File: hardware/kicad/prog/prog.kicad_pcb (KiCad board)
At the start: 4 copper layers, 174 x 134 mm, 124 parts, among them J1 AES_PROG, J2 Câble PROG-CHA, J3 PROG P, J4 PROG V, U1 AMS1117-3.3, U10 iCE40HX4K-TQ144, U11 W25Q32JVSS, U12 W9825G6KH-6, U13 iCE40HX4K-TQ144, U14 W25Q32JVSS, U15 W9825G6KH-6, U2 AP2112K-1.2, U3 74LVC16244A, U4 74LVC16244A, U5 74LVC16244A, U6 74LVC16245A, U7 74LVC16245A, U8 74AHCT125, U9 74LVC1G07, X1 25 MHz 3,3 V, X2 25 MHz 3,3 V

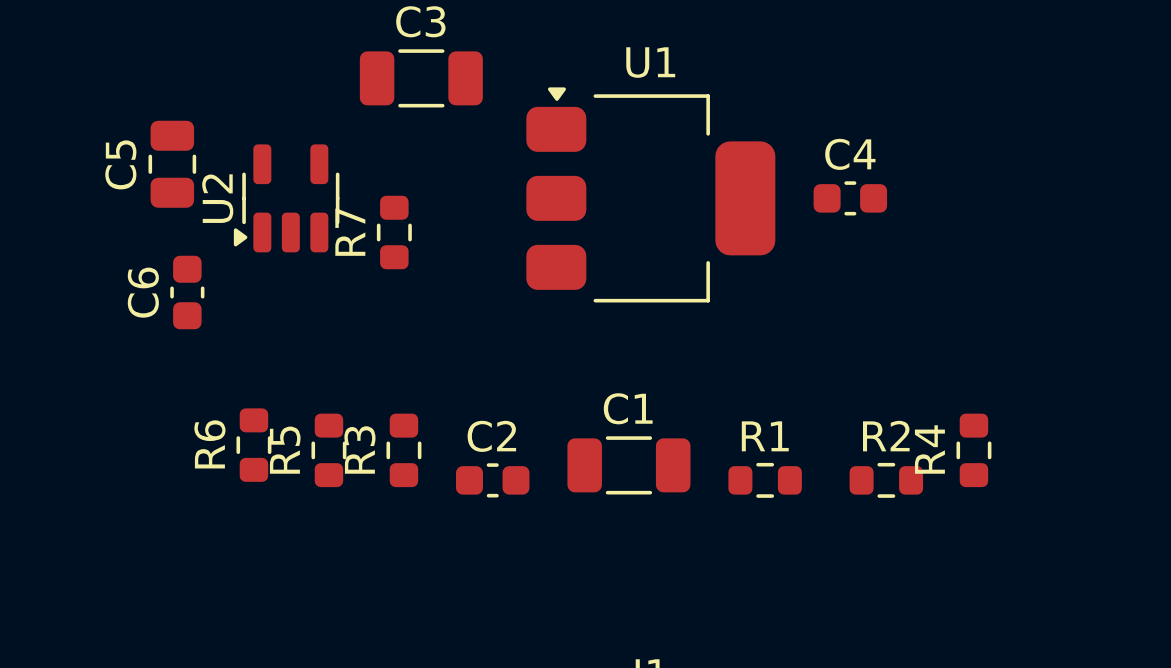
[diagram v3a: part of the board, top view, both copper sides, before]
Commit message: PCB : pistes et isolements de 0,127 mm
Premier routage 4 couches bloqué à 76 liaisons sur la carte PROG avec
0,15 mm ; 0,127 mm (5 mil) reste dans les capacités courantes des
fabricants en 4 couches.

Co-Authored-By: Claude Opus 5.5 <noreply@anthropic.com>
Claude-Session: https://claude.ai/code/session_01WKfXP1YJ8otGxZ5dsY6Agh
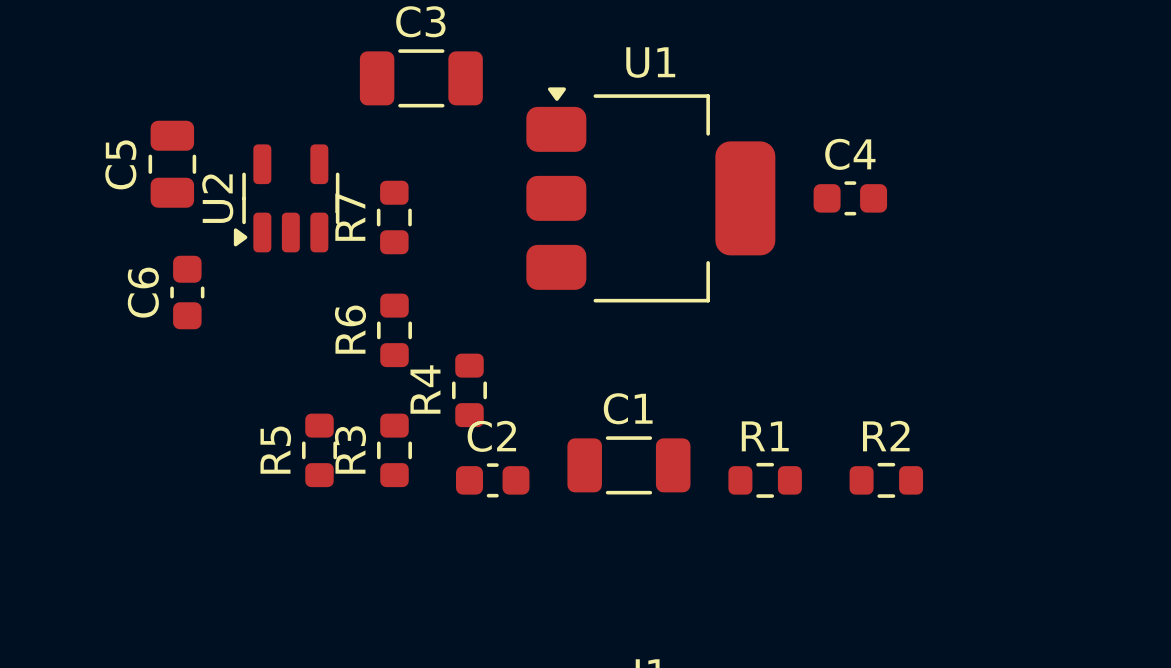
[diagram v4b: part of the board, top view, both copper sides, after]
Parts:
- moved R4 16.9 mm to (144.0, 156.4)
- moved R6 6.05 mm to (141.5, 154.4)
- moved R7 0.50 mm to (141.4, 150.6)
- moved R3 0.31 mm to (141.5, 158.4)
- moved R5 0.31 mm to (139.0, 158.4)

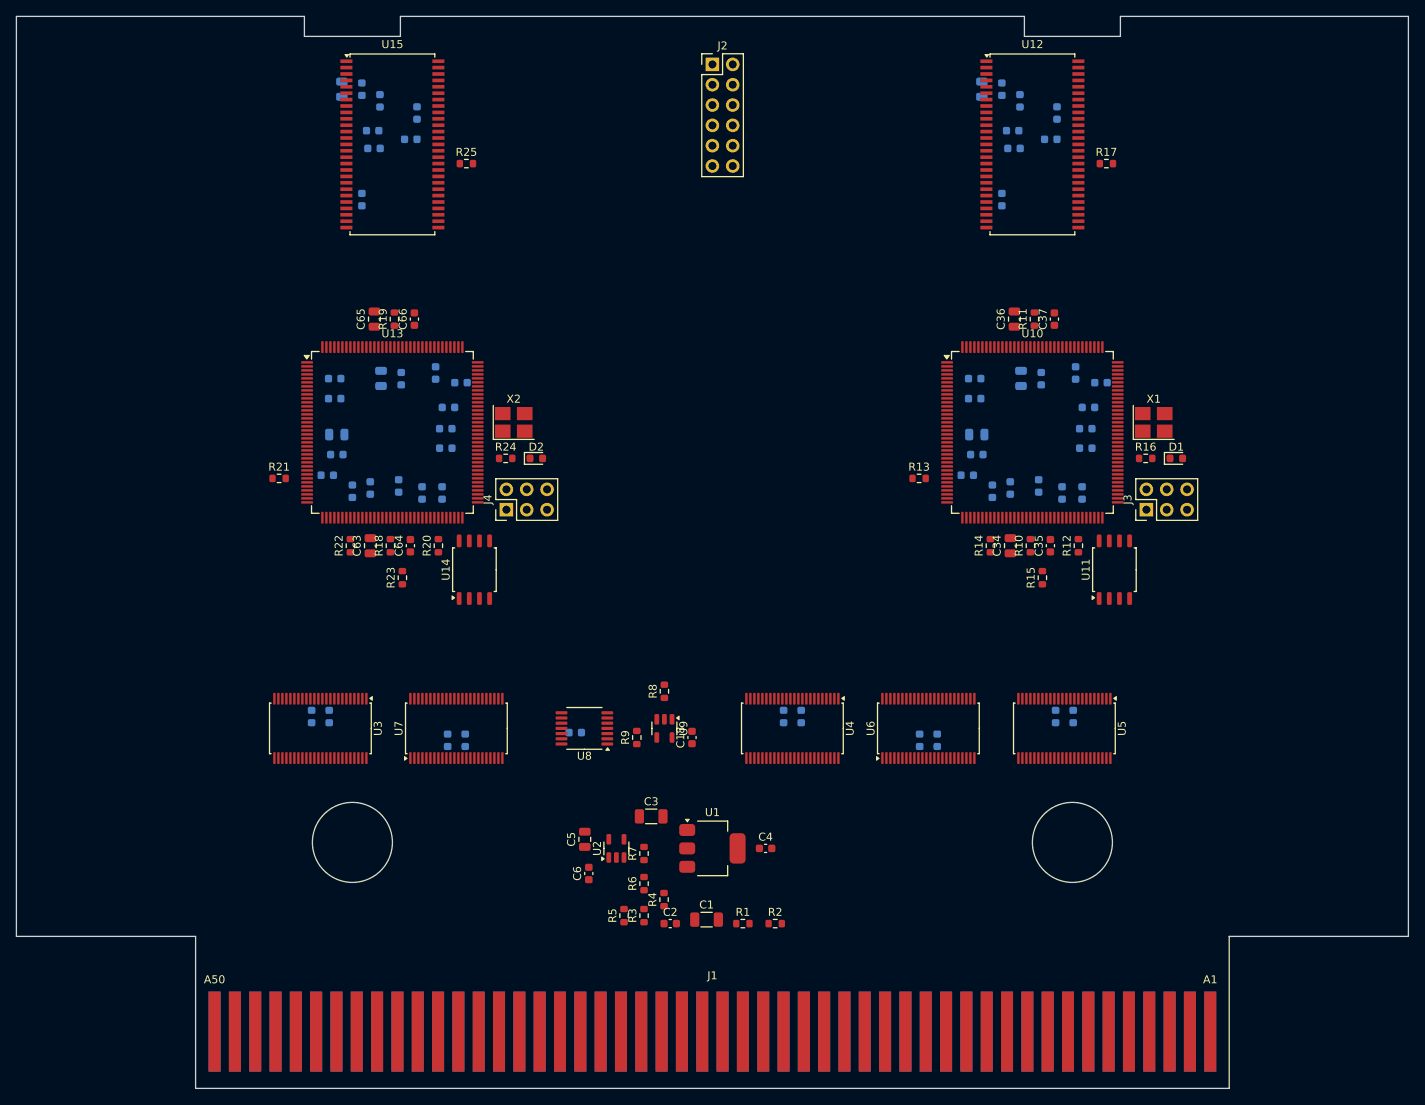
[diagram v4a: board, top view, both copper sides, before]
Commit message: PCB : 9 trous d'entretoise, vias vers les plans, zones interdites
- 9 trous M3 aux mêmes coordonnées sur PROG et CHA (H1-H9) pour relier
  les deux cartes par des entretoises ; 3,5 mm sans composant ni cuivre
  autour.
- Vias de raccordement aux plans (masse, +3V3) posés avant le routage
  pour chaque pastille CMS : au premier routage complet de la carte
  PROG, tous les signaux étaient routés et les 85 liaisons manquantes
  étaient toutes des raccordements aux plans.
- Zones interdites aux pistes autour des trous de la coque et des
  entretoises ; rétrécissement à 0,09 mm admis à l'entrée des broches.
- route.py : DRC par le module pcbnew (kicad-cli 7 n'en a pas), lecture
  de session corrigée.
- Pico descendu de 3 mm (chevauchait le lecteur microSD).

Co-Authored-By: Claude Opus 5.5 <noreply@anthropic.com>
Claude-Session: https://claude.ai/code/session_01WKfXP1YJ8otGxZ5dsY6Agh
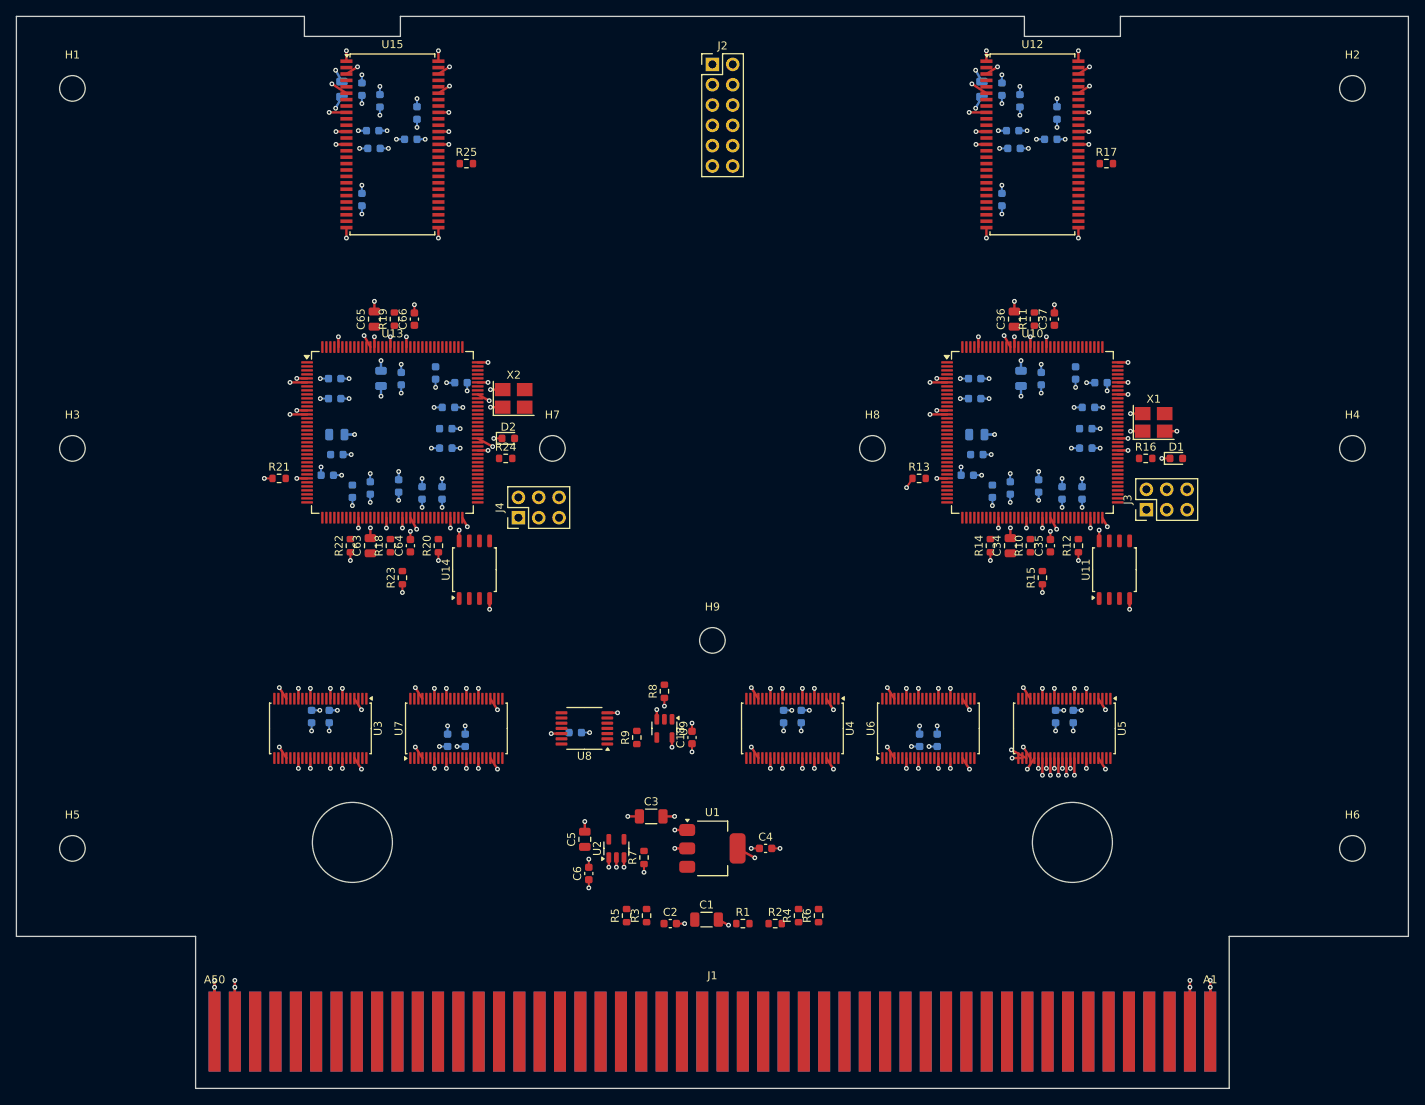
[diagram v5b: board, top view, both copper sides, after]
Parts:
- added H1: Entretoise M3, MountingHole:MountingHole_3.2mm_M3, F.Cu at (70.0, 55.0)
- added H2: Entretoise M3, MountingHole:MountingHole_3.2mm_M3, F.Cu at (230.0, 55.0)
- added H3: Entretoise M3, MountingHole:MountingHole_3.2mm_M3, F.Cu at (70.0, 100.0)
- added H4: Entretoise M3, MountingHole:MountingHole_3.2mm_M3, F.Cu at (230.0, 100.0)
- added H5: Entretoise M3, MountingHole:MountingHole_3.2mm_M3, F.Cu at (70.0, 150.0)
- added H6: Entretoise M3, MountingHole:MountingHole_3.2mm_M3, F.Cu at (230.0, 150.0)
- added H7: Entretoise M3, MountingHole:MountingHole_3.2mm_M3, F.Cu at (130.0, 100.0)
- added H8: Entretoise M3, MountingHole:MountingHole_3.2mm_M3, F.Cu at (170.0, 100.0)
- added H9: Entretoise M3, MountingHole:MountingHole_3.2mm_M3, F.Cu at (150.0, 124.0)
- moved R6 22.2 mm to (163.3, 158.4)
- moved R4 16.9 mm to (160.8, 158.4)
- moved D2 4.30 mm to (124.5, 98.8)
- moved X2 3.00 mm to (125.2, 93.8)
- moved J4 1.80 mm to (125.8, 108.7)
- moved R7 0.50 mm to (141.4, 151.1)
- moved R3 0.31 mm to (141.8, 158.4)
- moved R5 0.31 mm to (139.3, 158.4)
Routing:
- net GND: track 0.00 -> 270.9 mm, vias 0 -> 180
- net +3V3: track 0.00 -> 161.1 mm, vias 0 -> 129

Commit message: Routage : vias vers les plans verrouillés, Freerouting sans sortie des broches ni optimisation
L'import de la session effaçait aussi les vias vers les plans posés par
pcb.py (82 des 85 liaisons manquantes de la carte PROG) : ils sont
désormais verrouillés et conservés. Freerouting ne refait plus la
sortie des broches (près d'une heure perdue sur la carte CHA) ni
l'optimisation finale. Zones interdites limitées aux 4 couches
utilisées ; remplissage et DRC dans un processus à part (second
LoadBoard inutilisable dans le même processus).

Co-Authored-By: Claude Opus 5.5 <noreply@anthropic.com>
Claude-Session: https://claude.ai/code/session_01WKfXP1YJ8otGxZ5dsY6Agh
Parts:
- moved R4 18.0 mm to (143.0, 155.3), turned to 0 degrees
- moved R6 13.1 mm to (150.5, 155.3), turned to 0 degrees
- moved R5 6.74 mm to (143.0, 152.8), turned to 0 degrees
- moved R3 5.95 mm to (146.8, 155.3), turned to 0 degrees
- moved R7 1.50 mm to (141.4, 149.6)

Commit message: FPGA configurés par le RP2350 depuis la carte SD (plus de flash)
- Matériel : flash SPI retirées (4 W25Q32, 12 résistances, 4
  condensateurs). Le bus de liaison arrive sur les broches de
  configuration des iCE40 (LK_SCK -> 70 SCK, LK_IO[0] -> 68 SDI,
  LK_CS_N -> 71 SS), qui redeviennent ces entrées après le démarrage.
  CRESET_N commun aux 4 FPGA, tiré à la masse, piloté par le RP2350
  (GP28) ; câble PROG-CHA en 2 x 7 (CRESET_N + masse). Connecteur 2 x 3
  de secours par FPGA (iceprog -S).
- Firmware : fpga_boot.c (reset commun en mode SPI esclave, envoi des
  SDAES/fpga_*.bin l'un après l'autre, contrôle de CDONE) ; testé sur
  PC (bitstreams reçus à l'identique, FPGA laissés en reset si un
  fichier manque).
- make -C hdl sd : fichiers à copier sur la carte SD.
- PCB : table de placement et références des FPGA mises à jour,
  broches réoptimisées.
Placement-routage des FPGA avec les nouvelles broches : en cours.

Co-Authored-By: Claude Opus 5.5 <noreply@anthropic.com>
Claude-Session: https://claude.ai/code/session_01WKfXP1YJ8otGxZ5dsY6Agh
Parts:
- removed C75: 100n, Capacitor_SMD:C_0603_1608Metric
- removed C76: 10u, Capacitor_SMD:C_0805_2012Metric
- removed R20, R21, R22, R23: 10k, Resistor_SMD:R_0603_1608Metric
- removed R24: 470, Resistor_SMD:R_0603_1608Metric
- removed R25: 33, Resistor_SMD:R_0603_1608Metric
- removed U14: W25Q32JVSS, Package_SO:SOIC-8_5.23x5.23mm_P1.27mm
- removed U15: W9825G6KH-6, Package_SO:TSOP-II-54_22.2x10.16mm_P0.8mm
- C46, C51, C61, C64, C74: value 100n -> 10u; footprint Capacitor_SMD:C_0603_1608Metric -> Capacitor_SMD:C_0805_2012Metric
- C47, C52, C63, C65: value 10u -> 100n; footprint Capacitor_SMD:C_0805_2012Metric -> Capacitor_SMD:C_0603_1608Metric
- C62: moved to F.Cu
- C66: moved to B.Cu
- J2: footprint Connector_PinHeader_2.54mm:PinHeader_2x06_P2.54mm_Vertical -> Connector_PinHeader_2.54mm:PinHeader_2x07_P2.54mm_Vertical
- J3: value PROG P -> CONF P
- J4: value PROG V -> CONF V
- R13: value 10k -> 470
- R14: value 10k -> 33
- R15: value 10k -> 100
- R16: value 470 -> 100
- R17: value 33 -> 10k
- R18: value 100 -> 470
- R19: value 100 -> 33
- U11: value W25Q32JVSS -> W9825G6KH-6; footprint Package_SO:SOIC-8_5.23x5.23mm_P1.27mm -> Package_SO:TSOP-II-54_22.2x10.16mm_P0.8mm
- U12: value W9825G6KH-6 -> iCE40HX4K-TQ144; footprint Package_SO:TSOP-II-54_22.2x10.16mm_P0.8mm -> Package_QFP:TQFP-144_20x20mm_P0.5mm
- U13: value iCE40HX4K-TQ144 -> W9825G6KH-6; footprint Package_QFP:TQFP-144_20x20mm_P0.5mm -> Package_SO:TSOP-II-54_22.2x10.16mm_P0.8mm
- moved R17 96.2 mm to (115.8, 112.2), turned to 90 degrees
- moved R16 95.5 mm to (110.2, 83.8), turned to 90 degrees
- moved C47 92.7 mm to (103.1, 100.8), turned to 0 degrees
- moved U12 87.7 mm to (110.0, 98.0)
- moved R15 81.6 mm to (109.8, 112.2)
- moved U11 54.1 mm to (190.0, 62.0), turned to 0 degrees
- moved C39 51.0 mm to (186.2, 55.1)
- moved R14 49.9 mm to (199.2, 64.4), turned to 0 degrees
- moved C68 49.3 mm to (108.4, 56.5)
- moved C67 36.3 mm to (106.2, 55.1), turned to -90 degrees
- moved U13 36.0 mm to (110.0, 62.0)
- moved C64 28.7 mm to (107.8, 83.8)
- moved R13 28.5 mm to (204.2, 100.8)
- moved R19 21.4 mm to (119.2, 64.4), turned to 0 degrees
- moved C62 21.0 mm to (107.2, 112.2), turned to 90 degrees
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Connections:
- C47 pad 1: +3V3 -> +1V2
- C52 pad 1: +1V2 -> +3V3
- C62 pad 1: +3V3 -> V_VCCPLL0
- C64 pad 1: V_VCCPLL0 -> V_VCCPLL1
- C66 pad 1: V_VCCPLL1 -> +3V3
- J3 pad 1: P_FL_SCK -> PROG_SCK
- J3 pad 2: P_FL_CS_N -> CS_P
- J3 pad 3: P_FL_DI -> P_SDO
- J3 pad 4: P_FL_DO -> PROG_IO0
- J3 pad 5: P_CRESET_N -> CRESET_N
- J4 pad 1: V_FL_SCK -> PROG_SCK
- J4 pad 2: V_FL_CS_N -> CS_V
- J4 pad 3: V_FL_DI -> V_SDO
- J4 pad 4: V_FL_DO -> PROG_IO0
- J4 pad 5: V_CRESET_N -> CRESET_N
- R12 pad 1: +3V3 -> CRESET_N
- R12 pad 2: P_CRESET_N -> GND
- R13 pad 1: +3V3 -> P_LED
- R13 pad 2: P_FL_CS_N -> P_LED_K
- R14 pad 1: +3V3 -> P_SD_CLK
- R14 pad 2: P_FL_WP_N -> P_SD_CLK_R
- R15 pad 1: +3V3 -> +1V2
- R15 pad 2: P_FL_HOLD_N -> V_VCCPLL0
- R16 pad 1: P_LED -> +1V2
- R16 pad 2: P_LED_K -> V_VCCPLL1
- R17 pad 1: P_SD_CLK -> CRESET_N
- R17 pad 2: P_SD_CLK_R -> GND
- R18 pad 1: +1V2 -> V_LED
- R18 pad 2: V_VCCPLL0 -> V_LED_K
- R19 pad 1: +1V2 -> V_SD_CLK
- R19 pad 2: V_VCCPLL1 -> V_SD_CLK_R
- U10 pad 1: CS_P -> P_SD_A0
- U10 pad 10: MODE -> PROG_IO3
- U10 pad 101: P_SD_A9 -> P_SD_A6
- U10 pad 102: P_SD_A11 -> P_SD_A7
- U10 pad 104: P_SD_A12 -> P_SD_A8
- U10 pad 105: P_SD_CKE -> P_SD_A9
- U10 pad 106: P_SD_DQM1 -> P_SD_A11
- U10 pad 107: P_SD_DQ8 -> P_SD_A12
- U10 pad 11: PORTWEU_N -> MODE
- U10 pad 110: P_SD_DQ9 -> P_SD_CKE
- U10 pad 112: P_SD_DQ10 -> P_SD_DQM1
- U10 pad 113: P_SD_DQ11 -> P_SD_DQ8
- U10 pad 114: P_SD_DQ12 -> P_SD_DQ9
- U10 pad 115: P_SD_DQ13 -> P_SD_DQ10
- U10 pad 116: P_SD_DQ14 -> P_SD_DQ11
- U10 pad 117: P_SD_DQ15 -> P_SD_DQ12
- U10 pad 118: P_SD_DQ0 -> P_SD_DQ13
- U10 pad 119: P_SD_DQ1 -> P_SD_DQ14
- U10 pad 12: PORTWEL_N -> PORTWEU_N
- U10 pad 120: P_SD_DQ2 -> P_SD_DQ15
- U10 pad 121: P_SD_DQ3 -> P_SD_DQ0
- U10 pad 122: P_SD_DQ4 -> P_SD_DQ1
- U10 pad 124: P_SD_DQ5 -> P_SD_DQ2
- U10 pad 125: P_SD_DQ6 -> P_SD_DQ3
- U10 pad 128: P_SD_DQ7 -> P_SD_DQ4
- U10 pad 129: P_SD_DQM0 -> (no net)
- U10 pad 130: P_SD_WE_N -> P_SD_DQ5
- U10 pad 134: P_SD_CAS_N -> P_SD_DQ6
- U10 pad 135: P_SD_RAS_N -> P_SD_DQ7
- U10 pad 136: P_SD_CS_N -> P_SD_DQM0
- U10 pad 137: P_SD_BA0 -> P_SD_WE_N
- U10 pad 138: P_SD_BA1 -> P_SD_CAS_N
- U10 pad 139: P_SD_A10 -> P_SD_RAS_N
- U10 pad 141: P_SD_A0 -> P_SD_CS_N
- U10 pad 142: P_SD_A1 -> P_SD_BA0
- U10 pad 143: P_SD_A2 -> P_SD_BA1
- U10 pad 144: P_SD_A3 -> P_SD_A10
- U10 pad 15: PWAIT1_N -> PORTWEL_N
- U10 pad 16: PWAIT0_N -> PWAIT1_N
- U10 pad 17: ROMWAIT_N -> PWAIT0_N
- U10 pad 18: XLAT_EN_N -> ROMWAIT_N
- U10 pad 19: A7 -> XLAT_EN_N
- U10 pad 2: LK_IRQ -> P_SD_A1
- U10 pad 20: A8 -> A7
- U10 pad 21: A9 -> A8
- U10 pad 22: A10 -> A9
- U10 pad 23: A11 -> A10
- U10 pad 24: A12 -> A11
- U10 pad 25: A13 -> A12
- U10 pad 26: A14 -> A13
- U10 pad 28: A15 -> A14
- U10 pad 29: A16 -> A15
- U10 pad 3: PROG_IO0 -> P_SD_A2
- U10 pad 31: A17 -> A16
- U10 pad 32: A18 -> A17
- U10 pad 33: A19 -> A18
- U10 pad 34: ROMOE_N -> A19
- U10 pad 37: PORTOEU_N -> ROMOE_N
- U10 pad 38: PORTOEL_N -> PORTOEU_N
- U10 pad 39: D15 -> PORTOEL_N
- U10 pad 4: PROG_SCK -> P_SD_A3
- U10 pad 41: D14 -> D15
- U10 pad 42: D13 -> D14
- U10 pad 43: D12 -> D13
- U10 pad 44: D11 -> D12
- U10 pad 45: D10 -> D11
- U10 pad 47: D9 -> D10
- U10 pad 48: D8 -> D9
- U10 pad 49: D7 -> D8
- U10 pad 52: D6 -> D7
- U10 pad 55: D5 -> D6
- U10 pad 56: D4 -> D5
- U10 pad 60: D_DIR -> D4
- U10 pad 61: D3 -> D_DIR
- U10 pad 62: D2 -> D3
- U10 pad 63: D1 -> D2
- U10 pad 64: D0 -> D1
- U10 pad 66: P_CRESET_N -> CRESET_N
- U10 pad 67: P_FL_DI -> P_SDO
- U10 pad 68: P_FL_DO -> PROG_IO0
- U10 pad 7: PROG_IO2 -> LK_IRQ
- U10 pad 70: P_FL_SCK -> PROG_SCK
- U10 pad 71: P_FL_CS_N -> CS_P
- U10 pad 73: A1 -> D0
- U10 pad 74: A2 -> A1
- U10 pad 75: A3 -> A2
- U10 pad 76: A4 -> A3
- U10 pad 78: A5 -> A4
- U10 pad 79: A6 -> A5
- U10 pad 8: PROG_IO1 -> PROG_IO2
- U10 pad 80: (no net) -> A6
- U10 pad 84: P_LED -> (no net)
- U10 pad 87: (no net) -> P_LED
- U10 pad 9: PROG_IO3 -> PROG_IO1
- U10 pad 94: P_SD_CLK -> (no net)
- U10 pad 95: P_SD_A4 -> (no net)
- U10 pad 96: P_SD_A5 -> (no net)
- U10 pad 97: P_SD_A6 -> P_SD_CLK
- U10 pad 98: P_SD_A7 -> P_SD_A4
- U10 pad 99: P_SD_A8 -> P_SD_A5
- U11 pad 1: P_FL_CS_N -> +3V3
- U11 pad 2: P_FL_DO -> P_SD_DQ0
- U11 pad 3: P_FL_WP_N -> +3V3
- U11 pad 4: GND -> P_SD_DQ1
- U11 pad 5: P_FL_DI -> P_SD_DQ2
- U11 pad 6: P_FL_SCK -> GND
- U11 pad 7: P_FL_HOLD_N -> P_SD_DQ3
- U11 pad 8: +3V3 -> P_SD_DQ4
- U12 pad 1: +3V3 -> V_SD_BA0
- U12 pad 10: P_SD_DQ5 -> (no net)
- U12 pad 11: P_SD_DQ6 -> (no net)
- U12 pad 12: GND -> (no net)
- U12 pad 13: P_SD_DQ7 -> GND
- U12 pad 14: +3V3 -> GND
- U12 pad 15: P_SD_DQM0 -> (no net)
- U12 pad 16: P_SD_WE_N -> (no net)
- U12 pad 17: P_SD_CAS_N -> (no net)
- U12 pad 18: P_SD_RAS_N -> (no net)
- U12 pad 19: P_SD_CS_N -> (no net)
- U12 pad 2: P_SD_DQ0 -> V_SD_BA1
- U12 pad 20: P_SD_BA0 -> SDRMPX
- U12 pad 21: P_SD_BA1 -> SDPMPX
- U12 pad 22: P_SD_A10 -> (no net)
- U12 pad 23: P_SD_A0 -> (no net)
- U12 pad 24: P_SD_A1 -> (no net)
- U12 pad 25: P_SD_A2 -> (no net)
- U12 pad 26: P_SD_A3 -> (no net)
- U12 pad 27: +3V3 -> +1V2
- U12 pad 28: GND -> (no net)
- U12 pad 29: P_SD_A4 -> (no net)
- U12 pad 3: +3V3 -> V_SD_A10
- U12 pad 30: P_SD_A5 -> +3V3
- U12 pad 31: P_SD_A6 -> (no net)
- U12 pad 32: P_SD_A7 -> SDRA8
- U12 pad 33: P_SD_A8 -> SDRA9
- U12 pad 34: P_SD_A9 -> SDPA8
- U12 pad 35: P_SD_A11 -> (no net)
- U12 pad 36: P_SD_A12 -> (no net)
- U12 pad 37: P_SD_CKE -> SDRA20
- U12 pad 38: P_SD_CLK_R -> SDPA9
- U12 pad 39: P_SD_DQM1 -> SDRA21
- U12 pad 4: P_SD_DQ1 -> V_SD_A0
- U12 pad 40: (no net) -> +1V2
- U12 pad 41: GND -> SDPA10
- U12 pad 42: P_SD_DQ8 -> SDRA22
- U12 pad 43: +3V3 -> SDPA11
- U12 pad 44: P_SD_DQ9 -> SDRA23
- U12 pad 45: P_SD_DQ10 -> SDPOE_N
- U12 pad 46: GND -> +3V3
- U12 pad 47: P_SD_DQ11 -> SDROE_N
- U12 pad 48: P_SD_DQ12 -> RAD_DIR
- U12 pad 49: +3V3 -> SDRAD7
- U12 pad 5: P_SD_DQ2 -> GND
- U12 pad 50: P_SD_DQ13 -> (no net)
- U12 pad 51: P_SD_DQ14 -> (no net)
- U12 pad 52: GND -> SDRAD6
- U12 pad 53: P_SD_DQ15 -> GND
- U12 pad 54: GND -> V_VCCPLL0
- U12 pad 6: GND -> +3V3
- U12 pad 7: P_SD_DQ3 -> V_SD_A1
- U12 pad 8: P_SD_DQ4 -> V_SD_A2
- U12 pad 9: +3V3 -> V_SD_A3
- U13 pad 1: V_SD_CS_N -> +3V3
- U13 pad 10: V_SD_A3 -> V_SD_DQ5
- U13 pad 11: (no net) -> V_SD_DQ6
- U13 pad 12: (no net) -> GND
- U13 pad 13: GND -> V_SD_DQ7
- U13 pad 14: GND -> +3V3
- U13 pad 15: (no net) -> V_SD_DQM0
- U13 pad 16: (no net) -> V_SD_WE_N
- U13 pad 17: (no net) -> V_SD_CAS_N
- U13 pad 18: (no net) -> V_SD_RAS_N
- U13 pad 19: (no net) -> V_SD_CS_N
- U13 pad 2: V_SD_BA0 -> V_SD_DQ0
- U13 pad 20: SDRMPX -> V_SD_BA0
- U13 pad 21: SDPMPX -> V_SD_BA1
- U13 pad 22: (no net) -> V_SD_A10
- U13 pad 23: (no net) -> V_SD_A0
- U13 pad 24: (no net) -> V_SD_A1
- U13 pad 25: (no net) -> V_SD_A2
- U13 pad 26: (no net) -> V_SD_A3
- U13 pad 27: +1V2 -> +3V3
- U13 pad 28: (no net) -> GND
- U13 pad 29: (no net) -> V_SD_A4
- U13 pad 3: V_SD_BA1 -> +3V3
- U13 pad 30: +3V3 -> V_SD_A5
- U13 pad 31: (no net) -> V_SD_A6
- U13 pad 32: SDRA8 -> V_SD_A7
- U13 pad 33: SDRA9 -> V_SD_A8
- U13 pad 34: SDPA8 -> V_SD_A9
- U13 pad 35: (no net) -> V_SD_A11
- U13 pad 36: (no net) -> V_SD_A12
- U13 pad 37: SDRA20 -> V_SD_CKE
- U13 pad 38: SDPA9 -> V_SD_CLK_R
- U13 pad 39: SDRA21 -> V_SD_DQM1
- U13 pad 4: V_SD_A10 -> V_SD_DQ1
- U13 pad 40: +1V2 -> (no net)
- U13 pad 41: SDPA10 -> GND
- U13 pad 42: SDRA22 -> V_SD_DQ8
- U13 pad 43: SDPA11 -> +3V3
- U13 pad 44: SDRA23 -> V_SD_DQ9
- U13 pad 45: SDPOE_N -> V_SD_DQ10
- U13 pad 46: +3V3 -> GND
- U13 pad 47: SDROE_N -> V_SD_DQ11
- U13 pad 48: RAD_DIR -> V_SD_DQ12
- U13 pad 49: SDRAD7 -> +3V3
- U13 pad 5: GND -> V_SD_DQ2
- U13 pad 50: (no net) -> V_SD_DQ13
- U13 pad 51: (no net) -> V_SD_DQ14
- U13 pad 52: SDRAD6 -> GND
- U13 pad 53: GND -> V_SD_DQ15
- U13 pad 54: V_VCCPLL0 -> GND
- U13 pad 6: +3V3 -> GND
- U13 pad 7: V_SD_A0 -> V_SD_DQ3
- U13 pad 8: V_SD_A1 -> V_SD_DQ4
- U13 pad 9: V_SD_A2 -> +3V3
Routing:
- net +3V3: track 161.1 -> 147.0 mm, vias 129 -> 117
- net GND: track 270.9 -> 268.2 mm, vias 180 -> 178
